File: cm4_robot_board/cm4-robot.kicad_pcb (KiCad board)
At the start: 4 copper layers, 118 x 117 mm, 254 parts, among them J1 1747981-1, J10 Conn_01x04, J11 Conn_01x03, J12 Conn_01x04, J13 M12A-08PFFR-SF7003, J14 Power Sw, J15 I2C OLED, J2 M12A-08PFFR-SF7003, J21 Conn_01x03, J22 DNP, J23 Conn_01x01, J24 Conn_01x01, J25 RJ45, J3 USB_C_Receptacle_USB2.0, J4 Conn_01x04, J5 Conn_01x04, J6 Conn_01x04, J7 USB_A, J8 Conn_01x02, J9 ESTOP, Q1 Q_PMOS_GSD, Q10 Q_NMOS_GSD, Q2 Q_NMOS_GSD, Q3 Q_NMOS_GSD, Q4 Q_NMOS_GSD, Q5 Q_NMOS_GSD, Q6 AO3401A, Q7 AO3400A, Q8 Si2328DS, Q9 AO3401A, SW1 B3U-1000P, SW2 SW_SPDT, SW3 SW_SPDT, SW4 SW_SPDT, SW5 SW_SPDT, SW6 SW_DIP_x02, SW7 CONFIG_SW, U1 SN74LVC1G07QDCKTQ1, U10 isolator, U11 isolator, U12 TPS61040DBVR, U13 SC16IS752, U14 SC16IS752, U15 SN74LVC1G07QDCKTQ1, U16 CC56-12SEKWA, U17 ET6226M, U18 SN74LVC1G07QDCKTQ1, U19 SN74LVC1G07QDCKTQ1, U2 SN74LVC1G07QDCKTQ1, U20 TLV1117LV33DCYR, U21 FT231XS, U22 SN74LVC1G07QDCKTQ1, U23 TPD4E1U06DCKR, U24 ISL54222AIUZ, U25 USBLC6-2P6, U26 USBLC6-2P6, U27 SN74LVC1G07QDCKTQ1, U28 PCA9536D, U29 SN74LVC1G07QDCKTQ1, U3 LM2576HVS-5, U30 SN74LVC1G07QDCKTQ1, U31 LSM6DS3, U32 LIS3MDL, U33 ADS1115IDGS, U34 SN74LVC1G07QDCKTQ1, U35 SN74LVC1G07QDCKTQ1, U36 SN74LVC1G07QDCKTQ1, U4 TPD4E1U06DCKR, U5 ISL54222AIUZ, U6 LTC4412xS6, U7 TXS0101DCKR, U8 MCP2515-xSO, U9 MCP2515-xSO, Y1 16MHz, Y2 16MHz, Y3 14.7456MHz, Y4 14.7456MHz

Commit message: Motherboard: Add GPS port and other updates. Ready for review.
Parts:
- added J18: Serial Rear, Connector_PinSocket_2.54mm:PinSocket_2x05_P2.54mm_Vertical_SMD, B.Cu at (50.5, 119.0)
- moved J23 5.00 mm to (187.8, 61.0)
- moved J24 5.00 mm to (187.8, 95.0)
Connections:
- net Net-(J16-Pin_2) renamed /TX1
- net Net-(J16-Pin_3) renamed /RX1
- net Net-(J16-Pin_4) renamed /TX2
- net Net-(J16-Pin_5) renamed /RX2
- net Net-(J17-Pin_2) renamed /TX3
- net Net-(J17-Pin_3) renamed /RX3
- net Net-(J17-Pin_4) renamed /TX4
- net Net-(J17-Pin_5) renamed /RX4
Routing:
- net /RX2: track 52.2 -> 103.0 mm, vias 1 -> 2
- net /TX2: track 51.4 -> 99.2 mm, vias 1 -> 2
- net /TX4: track 73.6 -> 114.6 mm
- net /RX4: track 74.6 -> 115.6 mm, vias 1 -> 3
- net /RX1: track 49.0 -> 84.2 mm
- net /RX3: track 72.0 -> 102.3 mm, vias 1 -> 5
- net Net-(U2-Y): track 97.9 -> 120.5 mm, vias 2 -> 4
- net /TX1: track 46.2 -> 68.3 mm
- net /TX3: track 69.7 -> 90.4 mm, vias 1 -> 3
- net SERIALPWR1: track 55.0 -> 72.5 mm
- net /VMEAS: track 166.5 -> 157.2 mm, vias 10 -> 14
- net Net-(D4-K): track 70.4 -> 65.5 mm, vias 4 -> 2
- net GND: track 283.8 -> 287.8 mm, vias 171 -> 173
- net //LED_EN: track 167.9 -> 171.5 mm
- net Net-(D21-DOUT): track 159.2 -> 162.0 mm, vias 1 -> 3
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
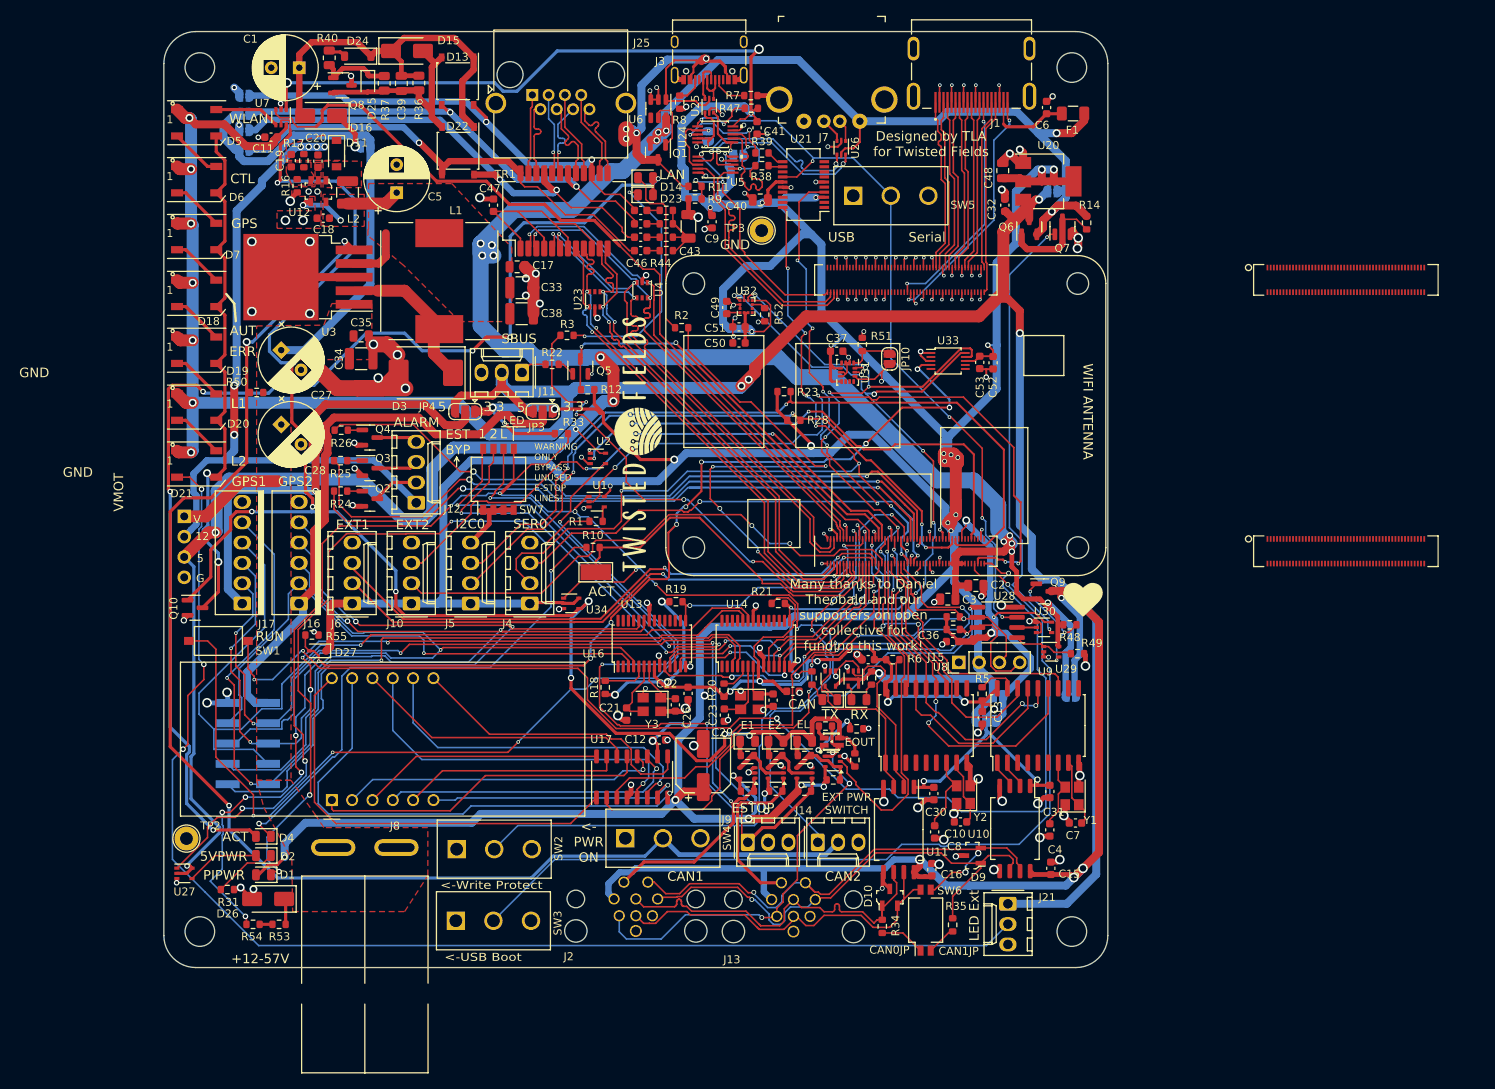
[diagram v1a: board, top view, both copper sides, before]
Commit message: update motherboard, add supercap_simple. ready for review
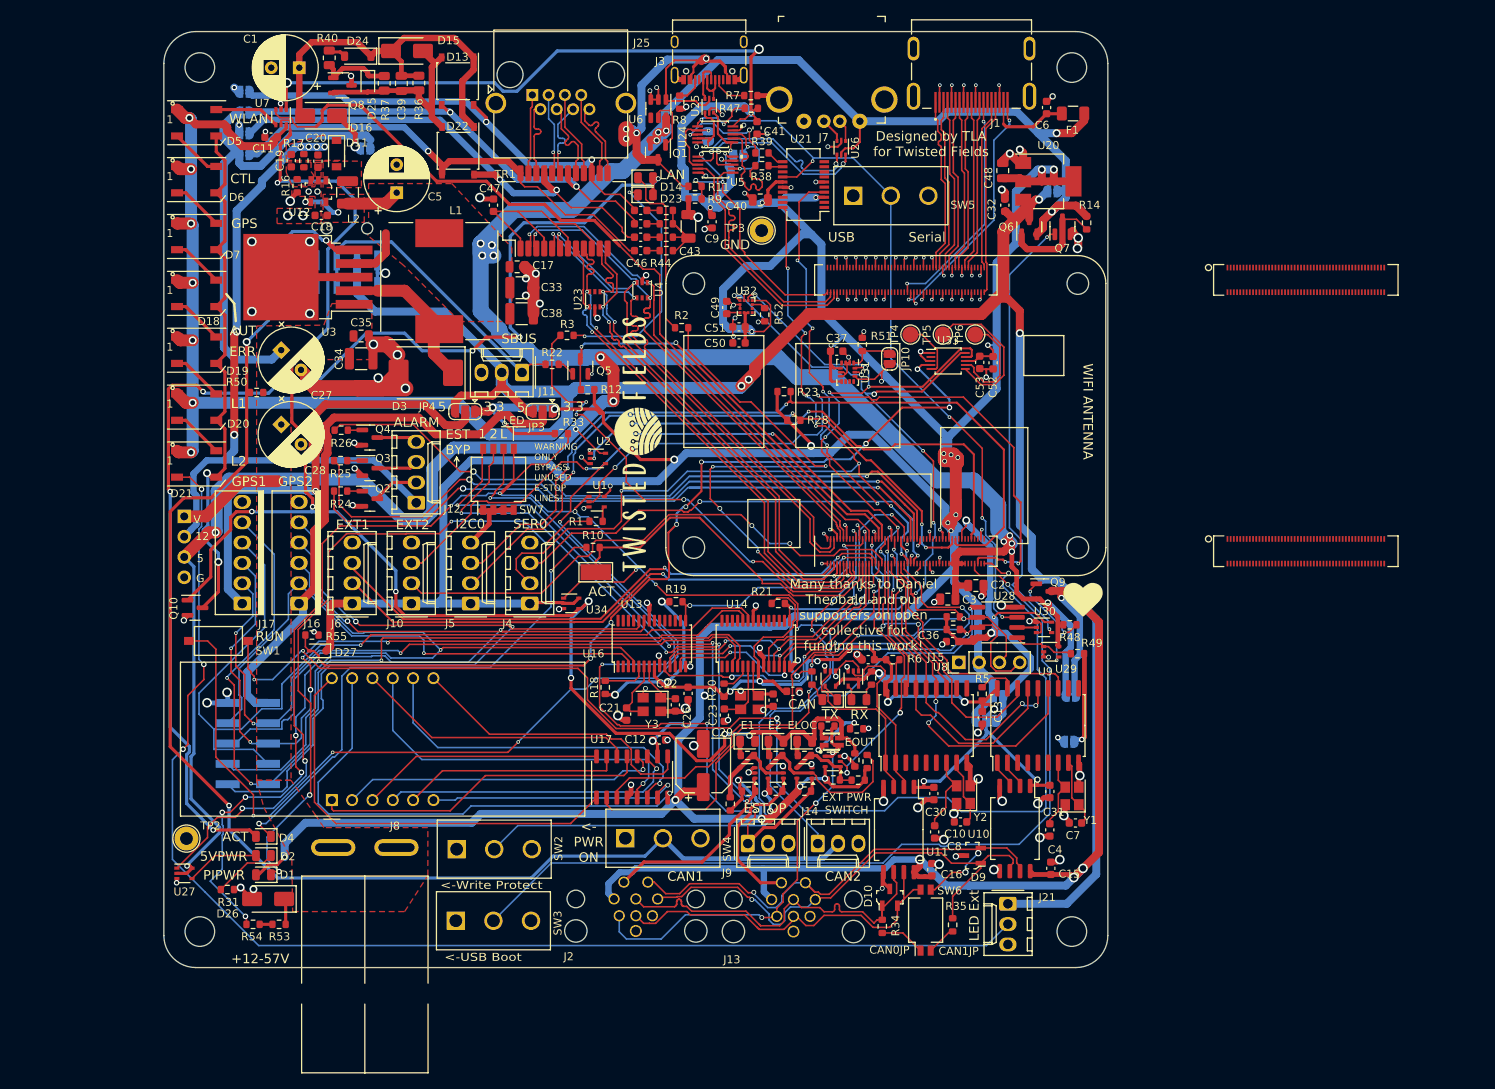
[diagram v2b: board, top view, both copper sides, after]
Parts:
- added J19: SBUS, parts:610108249221, B.Cu at (62.9, 54.7)
- added JP15: SolderJumper_2_Open, Jumper:SolderJumper-2_P1.3mm_Open_RoundedPad1.0x1.5mm, B.Cu at (153.2, 118.8)
- added R61: 10k, Resistor_SMD:R_0603_1608Metric, F.Cu at (110.8, 126.5)
- added R62: 10k, Resistor_SMD:R_0603_1608Metric, F.Cu at (127.9, 121.2)
- added R63: 10k, Resistor_SMD:R_0603_1608Metric, F.Cu at (126.8, 123.6)
- added TP4: TestPoint, TestPoint:TestPoint_Pad_D2.0mm, F.Cu at (133.3, 67.9)
- added TP5: TestPoint, TestPoint:TestPoint_Pad_D2.0mm, F.Cu at (137.4, 67.9)
- added TP6: TestPoint, TestPoint:TestPoint_Pad_D2.0mm, F.Cu at (141.4, 67.9)
- moved G*** 32.8 mm to (97.2, 52.8)
- moved G*** 32.8 mm to (95.6, 53.3)
- moved G*** 32.8 mm to (106.5, 52.8)
- moved J23 5.00 mm to (182.8, 61.0)
- moved J24 5.00 mm to (182.8, 95.0)
- moved JP11 0.55 mm to (50.1, 45.3)
- moved JP14 0.50 mm to (50.1, 37.5)
- moved C18 0.43 mm to (59.7, 53.0)
- moved JP12 0.40 mm to (50.1, 42.7)
- moved R60 0.30 mm to (123.0, 116.8)
- moved JP1 0.25 mm to (65.2, 44.6)
- moved J14 0.15 mm to (121.7, 131.5)
- moved J9 0.15 mm to (113.0, 131.5)
- moved R32 0.15 mm to (113.1, 124.9)
- moved JP13 0.15 mm to (50.1, 40.1)
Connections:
- R49 pad 2: GND -> Net-(JP15-A)
- U33 pad 5: unconnected-(U33-AIN1-Pad5) -> Net-(U33-AIN1)
- U33 pad 6: unconnected-(U33-AIN2-Pad6) -> Net-(U33-AIN2)
- U33 pad 7: unconnected-(U33-AIN3-Pad7) -> Net-(U33-AIN3)
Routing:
- net RC_SBUS: track 3.35 -> 38.1 mm
- net 5V_switched: track 323.0 -> 349.8 mm
- net Net-(U33-AIN2): track 0.00 -> 19.0 mm
- net Net-(U33-AIN3): track 0.00 -> 13.2 mm
- net Net-(U15-Y): track 7.61 -> 20.5 mm
- net Net-(JP15-A): track 0.00 -> 11.9 mm, vias 0 -> 1
- net ESTOP: track 47.2 -> 36.4 mm, vias 2 -> 4
- net +3V3: track 726.2 -> 734.3 mm
- net GND: track 287.8 -> 295.5 mm, vias 173 -> 174
- net Net-(U33-AIN1): track 0.00 -> 7.24 mm
- net GLOBAL_EN: track 152.3 -> 158.3 mm
- net /~{5V_EN}: track 171.9 -> 177.3 mm
- net Net-(U15-A): track 7.39 -> 11.6 mm
- net /LED_3.3V_POWER_NONINV: track 196.5 -> 193.3 mm
- net +5V: track 425.6 -> 423.2 mm
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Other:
- board text added: "5V CAN BOOT"
- board text added: "ELOC"
- board text added: "Radio"
- board text removed: "EL"
- board text removed: "VMOT"

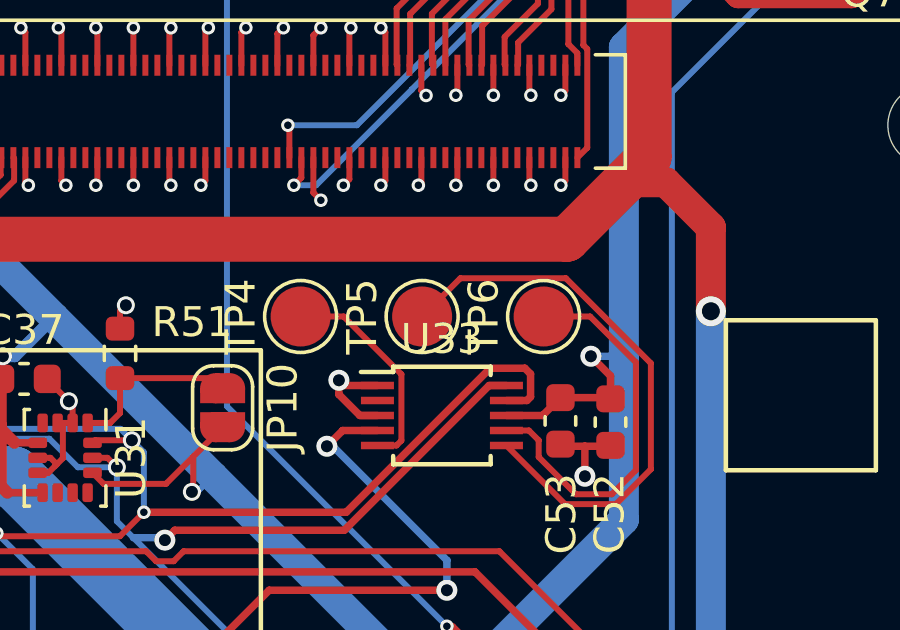
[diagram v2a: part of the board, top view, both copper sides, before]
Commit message: move CM4 connector off board to fix DRC errors, exclude other errors as appropriate
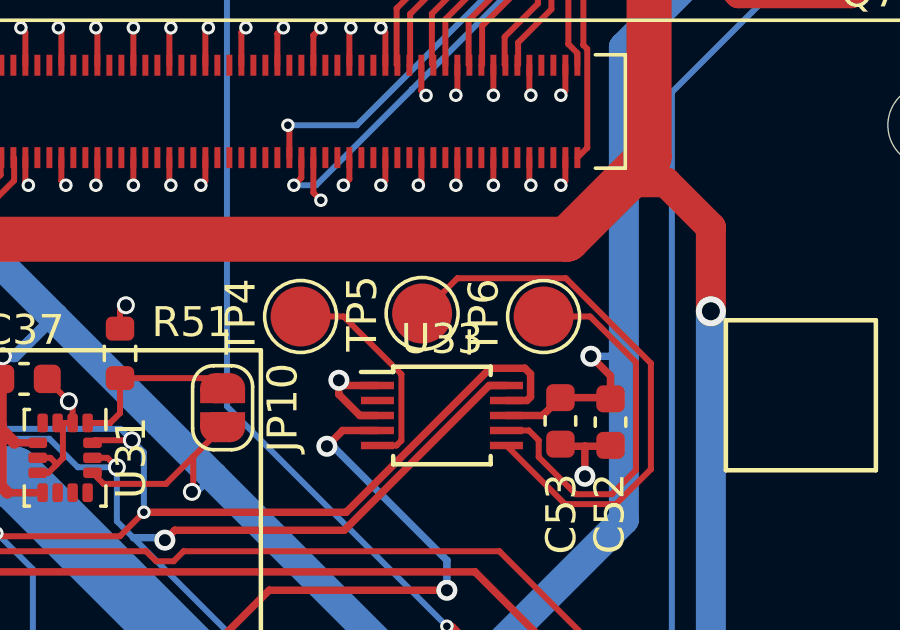
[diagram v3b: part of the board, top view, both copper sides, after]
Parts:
- moved TP5 0.10 mm to (137.4, 67.8)
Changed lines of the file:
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@@
 	(footprint "TestPoint:TestPoint_Pad_D2.0mm"
 		(layer "F.Cu")
-		(at 137.375 67.875 90)
+		(at 137.375 67.775 90)
 		(descr "SMD pad as test Point, diameter 2.0mm")
 		(tags "test point SMD pad")
@@
 	)
 	(segment
-		(start 140.185 72.175)
-		(end 142.14 74.13)
+		(start 142.14 74.13)
+		(end 143.83669 74.13)
 		(width 0.2)
 		(layer "F.Cu")
@@
 	)
 	(segment
-		(start 145 72.96669)
-		(end 145 69.43331)
+		(start 143.83669 74.13)
+		(end 145 72.96669)
 		(width 0.2)
 		(layer "F.Cu")
@@
 	)
 	(segment
-		(start 143.83669 74.13)
-		(end 145 72.96669)
+		(start 145 72.96669)
+		(end 145 69.43331)
 		(width 0.2)
 		(layer "F.Cu")
@@
 	)
 	(segment
-		(start 145 69.43331)
-		(end 142.16669 66.6)
+		(start 138.55 66.6)
+		(end 137.375 67.775)
 		(width 0.2)
 		(layer "F.Cu")
@@
 	)
 	(segment
-		(start 142.16669 66.6)
-		(end 138.65 66.6)
+		(start 145 69.43331)
+		(end 142.16669 66.6)
 		(width 0.2)
 		(layer "F.Cu")
@@
 	)
 	(segment
-		(start 138.65 66.6)
-		(end 137.375 67.875)
+		(start 142.16669 66.6)
+		(end 138.55 66.6)
 		(width 0.2)
 		(layer "F.Cu")
@@
 	)
 	(segment
-		(start 142.14 74.13)
-		(end 143.83669 74.13)
+		(start 140.185 72.175)
+		(end 142.14 74.13)
 		(width 0.2)
 		(layer "F.Cu")
